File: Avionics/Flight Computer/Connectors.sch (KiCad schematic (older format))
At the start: 3 parts, among them J1 ERF8-040-05.0-S-DV-K-TR, J2 ERF8-040-05.0-S-DV-K-TR, J3 473460001

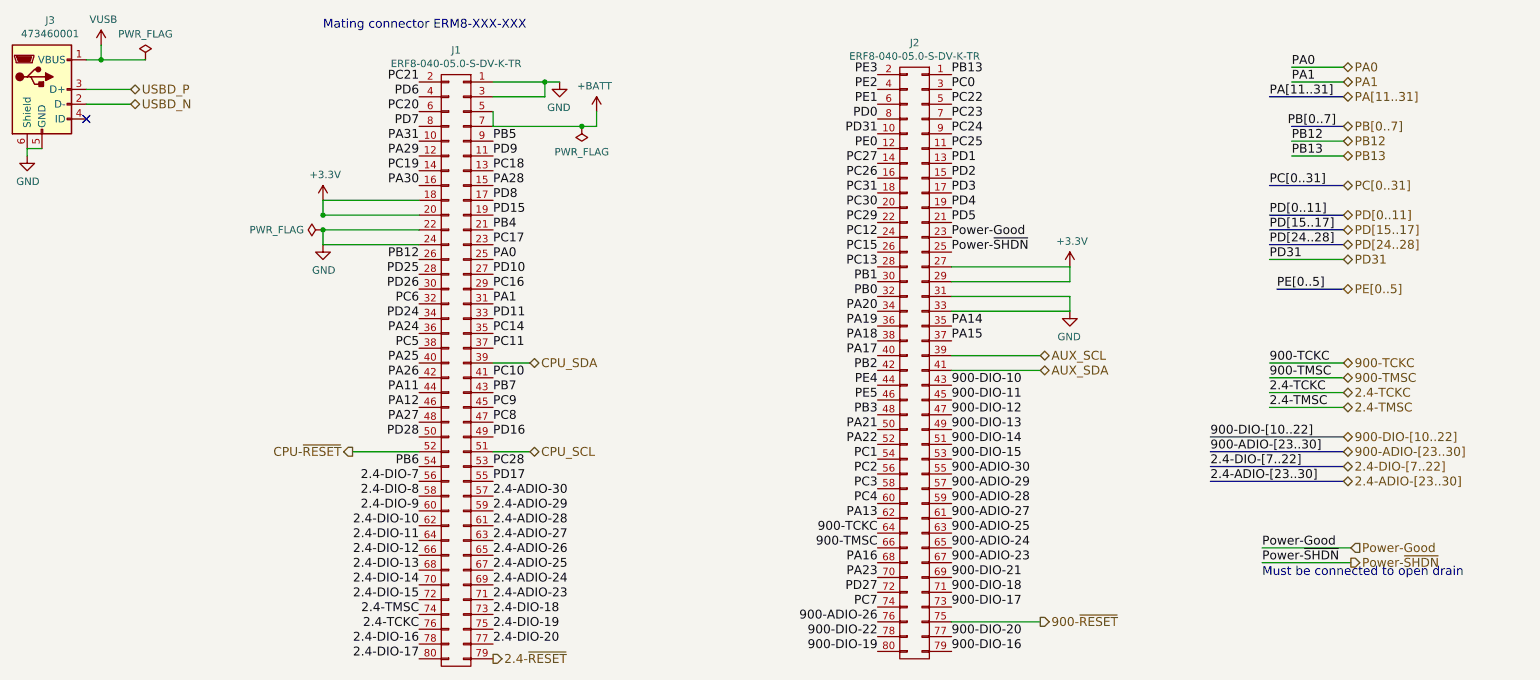
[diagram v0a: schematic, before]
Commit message: Finished rerouting and power supply update. Replaced connectors and did initial replacement.
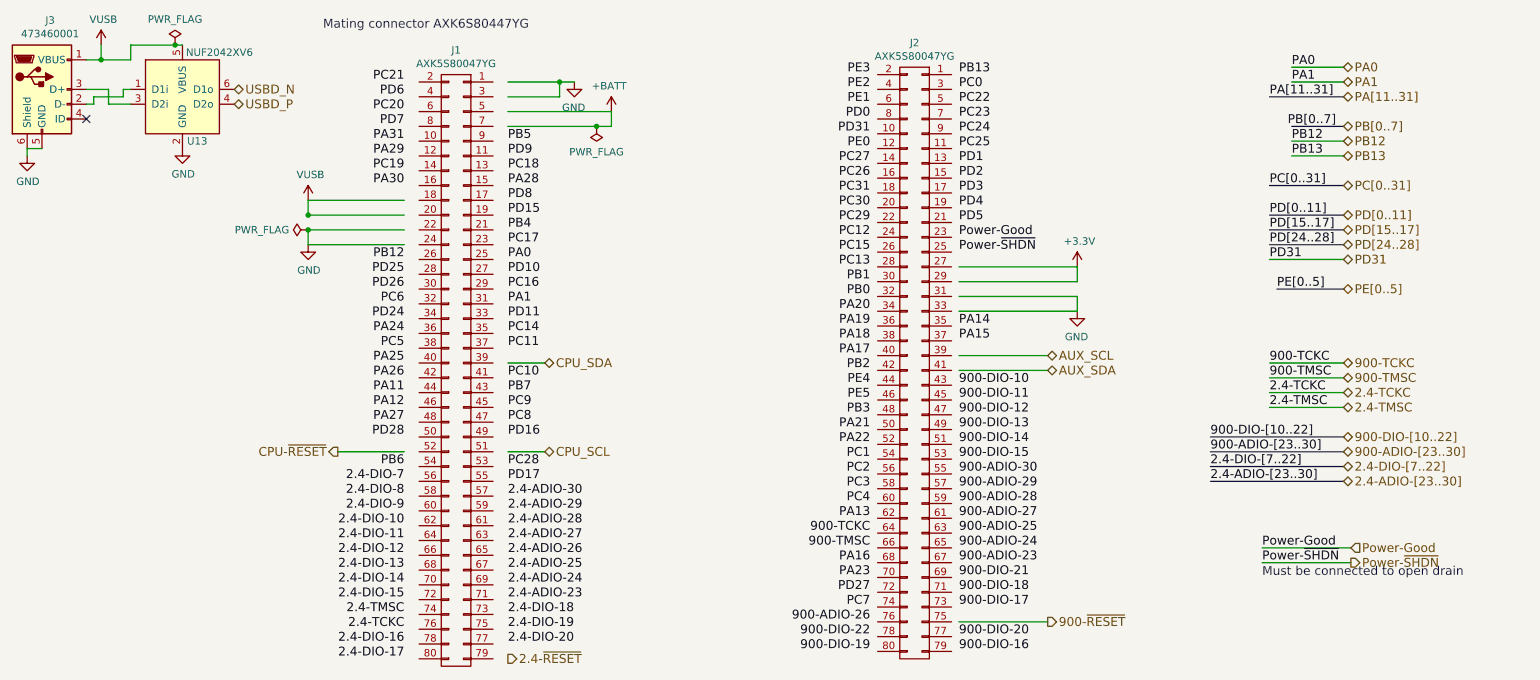
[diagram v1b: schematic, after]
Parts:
- added U13: NUF2042XV6, TO_SOT_Packages_SMD:SOT-563, symbol NUF2042XV6
- J1, J2: value ERF8-040-05.0-S-DV-K-TR -> AXK5S80047YG; footprint Connectors_Samtec:ERF8-040-05.0-S-DV-K -> Connectors:AXK5S80047YG
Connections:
- wire segments 41 -> 49
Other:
- note added: "Mating connector AXK6S80447YG"
- note removed: "Mating connector ERM8-XXX-XXX"

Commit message: Minor BOM fixes.
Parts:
- U13: value NUF2042XV6 -> NUF2042XV6T1G
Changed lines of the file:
@@
 P 2150 1500
 F 0 "U13" H 2250 1200 50  0000 C CNN
-F 1 "NUF2042XV6" H 2400 1800 50  0000 C CNN
+F 1 "NUF2042XV6T1G" H 2500 1800 50  0000 C CNN
 F 2 "TO_SOT_Packages_SMD:SOT-563" H 680 -725 50  0001 C CNN
 F 3 "http://www.onsemi.com/pub/Collateral/NUF2030XV6-D.PDF" H 600 -650 50  0001 C CNN
